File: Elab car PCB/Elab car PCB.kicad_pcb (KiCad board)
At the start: 2 copper layers, 139.8 x 134.2 mm, 86 parts, among them J1 USB_B, J10 I2C, J11 SCL pullup, J12 SDA pullup, J2 Power input, J3 L_Mot, J4 R_Mot, J5 HC-SR04, J6 R_Line, J7 L_Line, J8 Servo, J9 MPU5060, Q1 S8050, Q2 S8050, Q3 2N7000, Q4 2N7000, SW1 Reset, SW2 User 1, SW3 User 2, U1 CH340G, U2 L293D, U3 AMS1117-3.3, U4 ESP32-WROOM-32, U5 L7805, Y1 12MHz

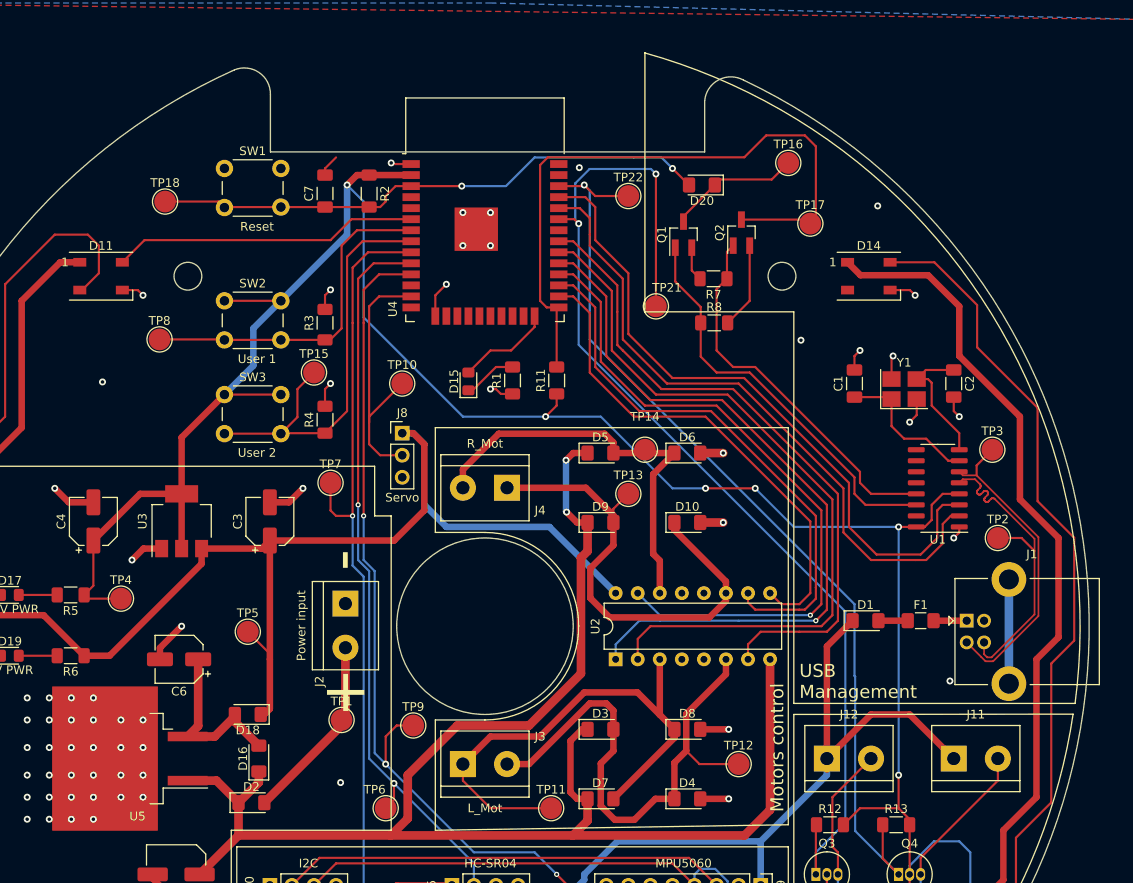
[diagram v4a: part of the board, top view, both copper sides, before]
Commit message: Front silk screen adjustment
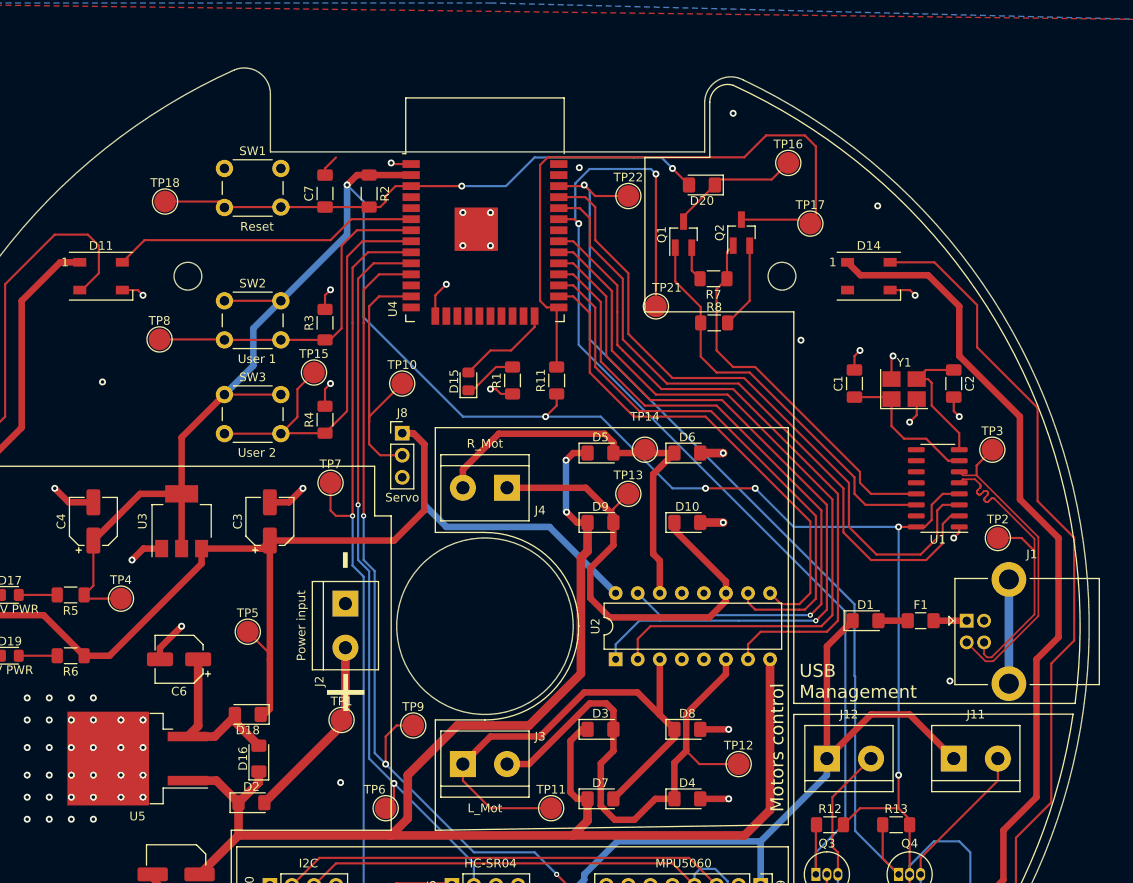
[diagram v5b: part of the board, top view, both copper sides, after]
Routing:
- net GND: vias 71 -> 72

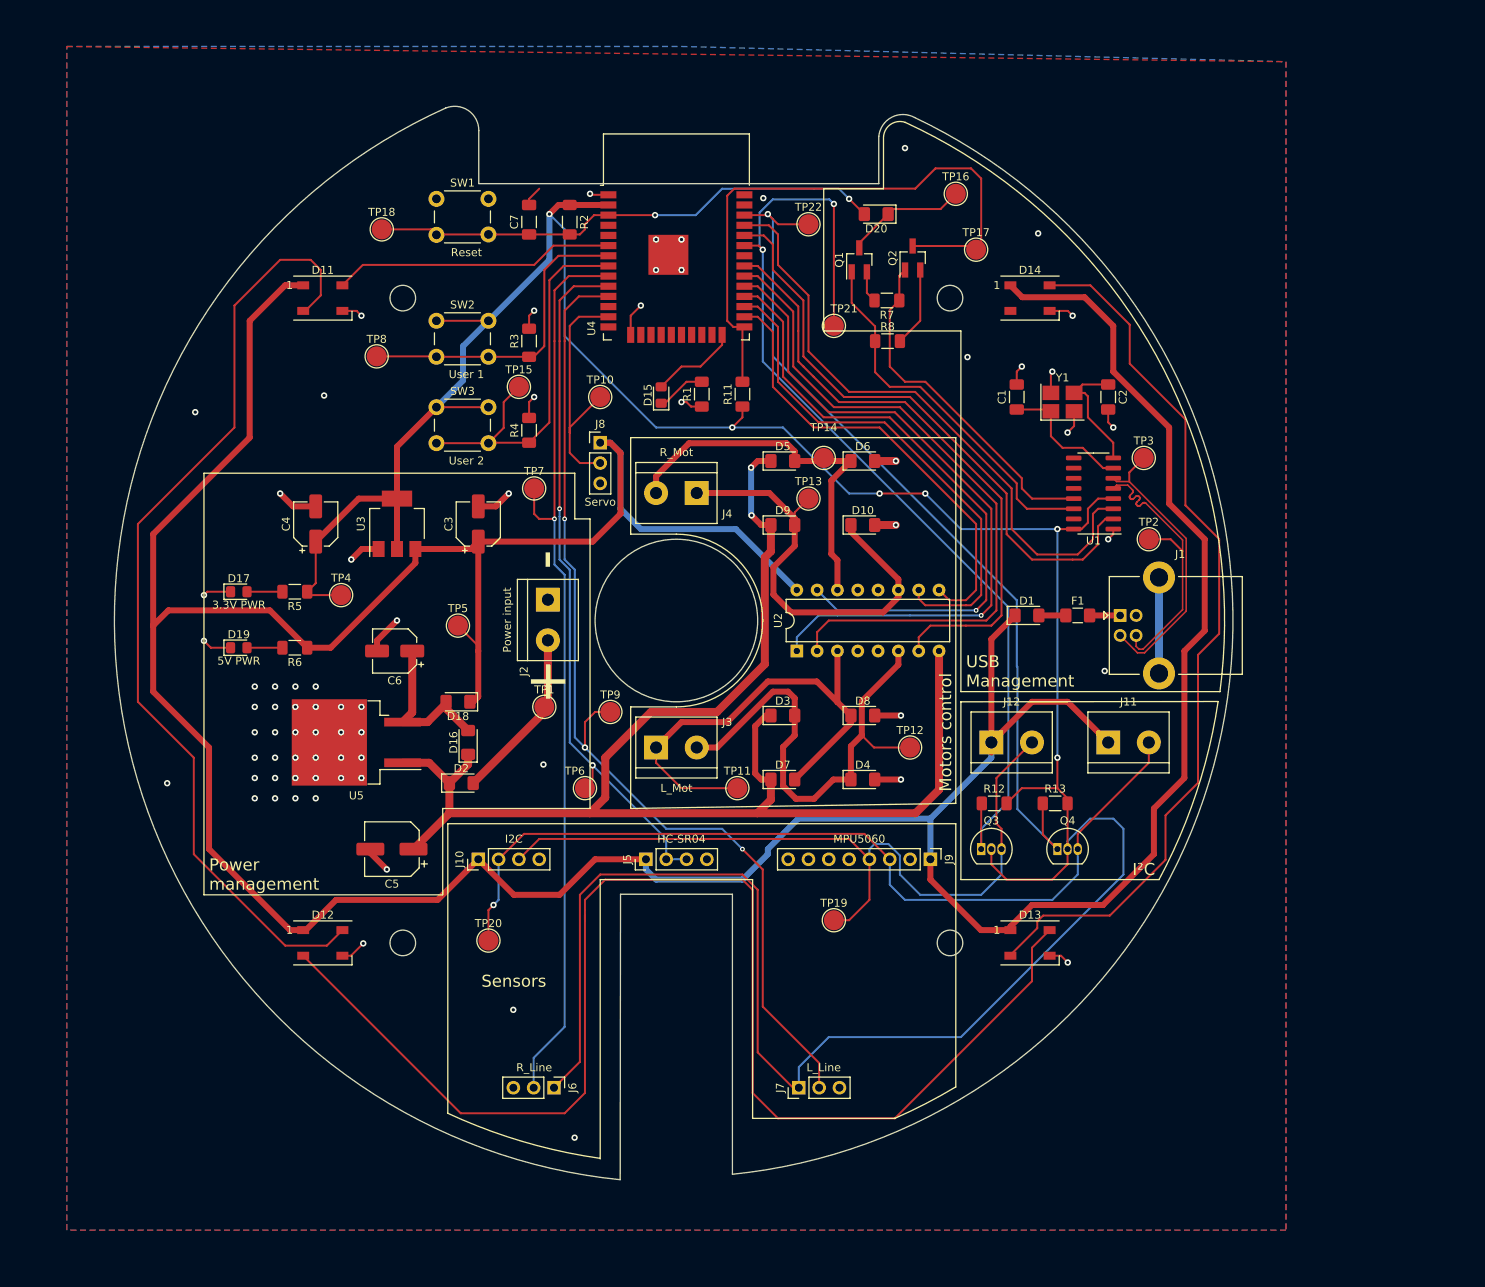
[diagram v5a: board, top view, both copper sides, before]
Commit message: Adding gnd vias
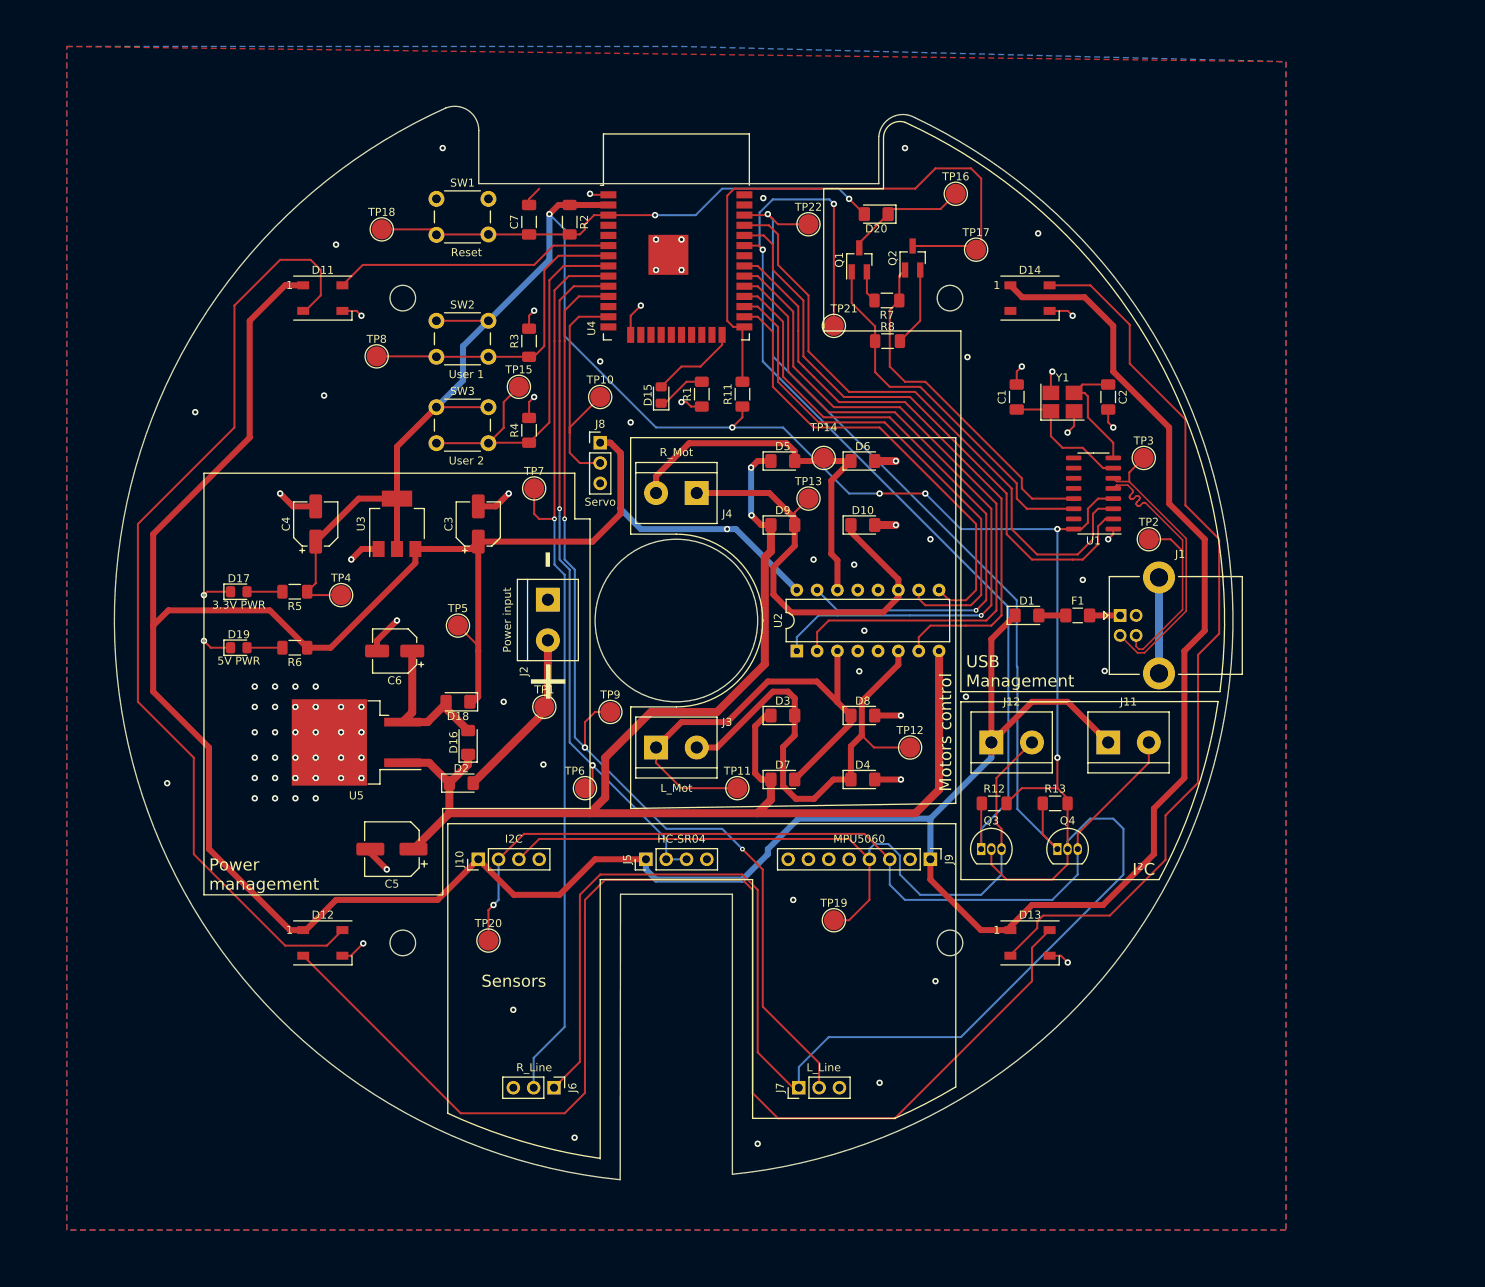
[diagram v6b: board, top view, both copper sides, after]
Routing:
- net GND: vias 72 -> 88
- net +5V: vias 0 -> 1
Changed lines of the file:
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@@
     (thickness 1.6)
     (drawings 60)
-    (tracks 903)
+    (tracks 921)
     (zones 0)
     (modules 86)
@@
   (via (at 95.66402 73.47712) (size 0.8) (drill 0.4) (layers F.Cu B.Cu) (net 1))
   (via (at 168.275 42.545) (size 0.8) (drill 0.4) (layers F.Cu B.Cu) (net 1))
+  (via (at 190.5 96.52) (size 0.8) (drill 0.4) (layers F.Cu B.Cu) (net 1))
+  (via (at 154.305 136.525) (size 0.8) (drill 0.4) (layers F.Cu B.Cu) (net 1))
+  (via (at 165.1 159.385) (size 0.8) (drill 0.4) (layers F.Cu B.Cu) (net 1))
+  (via (at 172.085 146.685) (size 0.8) (drill 0.4) (layers F.Cu B.Cu) (net 1))
+  (via (at 149.86 167.005) (size 0.8) (drill 0.4) (layers F.Cu B.Cu) (net 1))
+  (via (at 175.895 111.125) (size 0.8) (drill 0.4) (layers F.Cu B.Cu) (net 1))
+  (via (at 162.56 107.95) (size 0.8) (drill 0.4) (layers F.Cu B.Cu) (net 1))
+  (via (at 163.195 102.87) (size 0.8) (drill 0.4) (layers F.Cu B.Cu) (net 1))
+  (via (at 161.925 94.615) (size 0.8) (drill 0.4) (layers F.Cu B.Cu) (net 1))
+  (via (at 156.845 93.98) (size 0.8) (drill 0.4) (layers F.Cu B.Cu) (net 1))
+  (via (at 171.45 91.44) (size 0.8) (drill 0.4) (layers F.Cu B.Cu) (net 1))
+  (via (at 133.985 76.835) (size 0.8) (drill 0.4) (layers F.Cu B.Cu) (net 1))
+  (via (at 130.175 69.215) (size 0.8) (drill 0.4) (layers F.Cu B.Cu) (net 1))
+  (via (at 110.49 42.545) (size 0.8) (drill 0.4) (layers F.Cu B.Cu) (net 1))
+  (via (at 97.155 54.61) (size 0.8) (drill 0.4) (layers F.Cu B.Cu) (net 1))
+  (via (at 118.11 111.76) (size 0.8) (drill 0.4) (layers F.Cu B.Cu) (net 1))
   (segment (start 186.2875 75.2225) (end 186.51 75.445) (width 0.25) (layer F.Cu) (net 2))
   (segment (start 182.245 75.2225) (end 186.2875 75.2225) (width 0.25) (layer F.Cu) (net 2))
@@
   (segment (start 171.45 133.985) (end 177.765 140.3) (width 0.75) (layer F.Cu) (net 4))
   (segment (start 154.7495 97.79) (end 147.1295 90.17) (width 0.75) (layer B.Cu) (net 4))
-  (segment (start 147.1295 90.17) (end 135.255 90.17) (width 0.75) (layer B.Cu) (net 4))
+  (segment (start 147.1295 90.17) (end 146.05 90.17) (width 0.75) (layer B.Cu) (net 4))
   (segment (start 135.255 90.17) (end 132.715 87.63) (width 0.75) (layer B.Cu) (net 4))
   (segment (start 132.715 87.63) (end 132.715 80.645) (width 0.75) (layer B.Cu) (net 4))
@@
   (segment (start 114.935 105.41) (end 114.935 91.735) (width 0.75) (layer F.Cu) (net 4))
   (segment (start 114.935 111.125) (end 114.935 105.41) (width 0.75) (layer F.Cu) (net 4))
+  (segment (start 146.05 90.17) (end 135.255 90.17) (width 0.75) (layer B.Cu) (net 4))
+  (via (at 146.05 90.17) (size 0.8) (drill 0.4) (layers F.Cu B.Cu) (net 4))
   (segment (start 116.205 64.135) (end 109.705 64.135) (width 0.25) (layer F.Cu) (net 5))
   (segment (start 109.705 74.93) (end 116.205 74.93) (width 0.25) (layer F.Cu) (net 5))

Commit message: V1.1
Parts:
- removed TP1, TP11, TP12, TP13, TP14, TP16, TP2, TP3: TestPoint, TestPoint:TestPoint_Pad_D2.5mm
- added H1: MountingHole, MountingHole:MountingHole_3.2mm_M3_DIN965_Pad, F.Cu at (105.5, 61.3)
- added H2: MountingHole, MountingHole:MountingHole_3.2mm_M3_DIN965_Pad, F.Cu at (105.5, 141.9)
- added H3: MountingHole, MountingHole:MountingHole_3.2mm_M3_DIN965_Pad, F.Cu at (173.9, 141.9)
- added H4: MountingHole, MountingHole:MountingHole_3.2mm_M3_DIN965_Pad, F.Cu at (173.9, 61.3)
- added J13: Conn_01x03, Connector_PinHeader_2.54mm:PinHeader_1x03_P2.54mm_Vertical, F.Cu at (96.5, 74.9)
- added SW4: SW_DIP_x01, electroLABOT_switch:SW_plugin8.5x8.5, F.Cu at (118.7, 114.3)
- J6: value R_Line -> Conn_01x04; footprint Connector_PinHeader_2.54mm:PinHeader_1x03_P2.54mm_Vertical -> Connector_PinHeader_2.54mm:PinHeader_1x04_P2.54mm_Vertical
- J7: value L_Line -> Conn_01x04; footprint Connector_PinHeader_2.54mm:PinHeader_1x03_P2.54mm_Vertical -> Connector_PinHeader_2.54mm:PinHeader_1x04_P2.54mm_Vertical
- J9: value MPU5060 -> MPU6050
- R1: value 85R -> 20R
- R5: value 20R -> 100R
- R6: value 85r -> 200R
- moved J7 12.2 mm to (167.0, 158.1), turned to 270 degrees
- moved R7 5.84 mm to (164.8, 67.3)
- moved D15 5.08 mm to (142.9, 73.3)
- moved J6 4.77 mm to (120.0, 158.1)
- moved R8 4.62 mm to (164.8, 62.2)
- moved R1 3.18 mm to (146.1, 73.3)
- moved R11 1.91 mm to (149.9, 73.3)
- moved Q1 1.42 mm to (161.3, 57.1)
- moved Q2 1.29 mm to (168.3, 57.1)
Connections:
- J2 pad 2: Net-(D2-Pad2) -> Net-(J2-Pad2)
- J6 pad 1: +3V3 -> /line_sens_1
- J6 pad 2: /line_sens_1 -> (no net)
- J7 pad 1: +3V3 -> /line_sens_2
- J7 pad 2: /line_sens_2 -> (no net)
- J8 pad 1: +5V -> /servo_sig
- J8 pad 2: /servo_sig -> +5V
- Q1 pad 1: /RTS -> Net-(Q1-Pad1)
- Q1 pad 2: Net-(Q1-Pad2) -> /RTS
- Q2 pad 1: /DTR -> Net-(Q2-Pad1)
- Q2 pad 2: Net-(Q2-Pad2) -> /DTR
- R7 pad 2: Net-(Q1-Pad2) -> Net-(Q1-Pad1)
- R8 pad 2: Net-(Q2-Pad2) -> Net-(Q2-Pad1)
- U4 pad 10: /dist_sensor -> /BP_2
- U4 pad 11: /line_sens_2 -> /line_sens_1
- U4 pad 12: (no net) -> /dist_sensor
- U4 pad 13: /servo_sig -> /line_sens_2
- U4 pad 16: (no net) -> /servo_sig
- U4 pad 23: (no net) -> /piezo
- U4 pad 6: /WS_sig -> (no net)
- U4 pad 7: /BP_1 -> (no net)
- U4 pad 8: /BP_2 -> /WS_sig
- U4 pad 9: /line_sens_1 -> /BP_1
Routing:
- net /piezo: track 0.00 -> 53.7 mm, vias 0 -> 1
- net Net-(J2-Pad2): track 0.00 -> 17.3 mm
- net /servo_sig: track 31.5 -> 15.6 mm
- net +3V3: track 403.0 -> 413.5 mm
- net Net-(Q2-Pad2): track 9.94 -> 0.00 mm
- net Net-(Q1-Pad1): track 0.00 -> 9.87 mm
- net Net-(D2-Pad2): track 21.8 -> 14.0 mm
- net Net-(D20-Pad1): track 15.2 -> 7.79 mm
- net /line_sens_2: track 127.5 -> 132.9 mm
- net /D+: track 37.5 -> 32.6 mm
- net +5V: track 512.6 -> 508.2 mm
- net /line_sens_1: track 115.3 -> 111.2 mm
- net Net-(Q1-Pad2): track 3.98 -> 0.00 mm
- net Net-(Q2-Pad1): track 0.00 -> 3.98 mm
- net /D-: track 36.3 -> 32.6 mm
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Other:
- board text added: "Piezo"
- board text added: "S"
- board text added: "electroLABOT V1.1 Yann Jacquet - electroLAB - UMONS 2021-12-21"
- board text removed: "electroLABOT V1.0 Yann Jacquet - electroLAB - UMONS 2021-09-21"

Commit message: Little corrections of V1.1
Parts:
- J9: value MPU6050 -> MPU5060
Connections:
- J13 pad 2: (no net) -> +5V
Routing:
- net +5V: track 508.2 -> 522.3 mm, vias 1 -> 0
- net GND: vias 85 -> 127
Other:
- board text added: "HC-SR04"
- board text added: "I2C"
- board text added: "I2C pullups"
- board text added: "Left motor"
- board text added: "Line sensor 1"
- board text added: "Line sensor 2"
- board text added: "MPU6050"
- board text added: "Power"
- board text added: "Reset"
- board text added: "Rigth motor"
- board text added: "User 1"
- board text added: "User 2"
